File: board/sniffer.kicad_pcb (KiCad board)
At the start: 8 copper layers, 154 x 125 mm, 314 parts, among them J1 BARREL, J10 CONN_SFP_HOST, J11 SFP_CAGE, J12 PMOD_HOST, J13 CONN_SATA_DEVICE, J14 CONN_SATA_HOST, J15 CONN_LVDS_EXPANSION_HOST, J2 32K243-40ML5, J3 BEL_FUSE_0826-1G1T-23-F, J4 XILINX_JTAG, J5 32K243-40ML5, J6 32K243-40ML5, J7 32K243-40ML5, J8 CONN_SFF8087, J9 CONN_SFF8087, M1 SCREW_HOLE, M2 SCREW_HOLE, M3 SCREW_HOLE, M4 SCREW_HOLE, Q1 SSM6N58NU, U1 OKL-T_3-W12P-C, U10 KSZ9031RN, U11 74AVCH1T45, U12 74AVCH1T45, U13 74AVCH1T45, U14 74AVCH1T45, U15 W25Q128JV, U16 FPF2498, U17 FPF2498, U18 LP2996A, U2 LTC3374-QFN, U3 MYTNA1R84RELA2RA, U4 DDR3_SODIMM, U5 XC7K70T-2FBG484, U6 ECX2-LMV-7CN-156.250-TR, U7 ECX2-LMV-3CN-125.000-TR, U8 ECX2-LMV-3CN-125.000-TR, U9 ECS-2016MVQ-250-CN

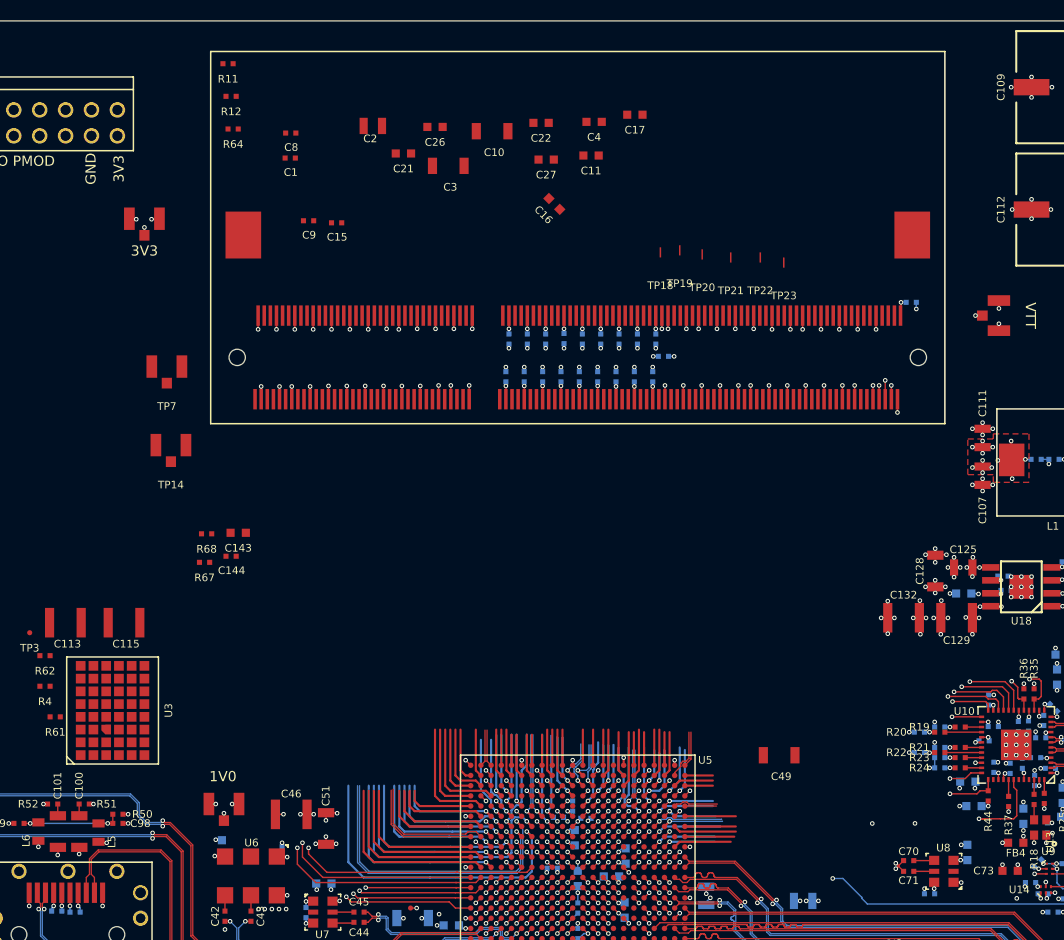
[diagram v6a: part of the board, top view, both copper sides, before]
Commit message: Preliminary layout of DQ byte groups 3:0 on DDR3. Not length matched.
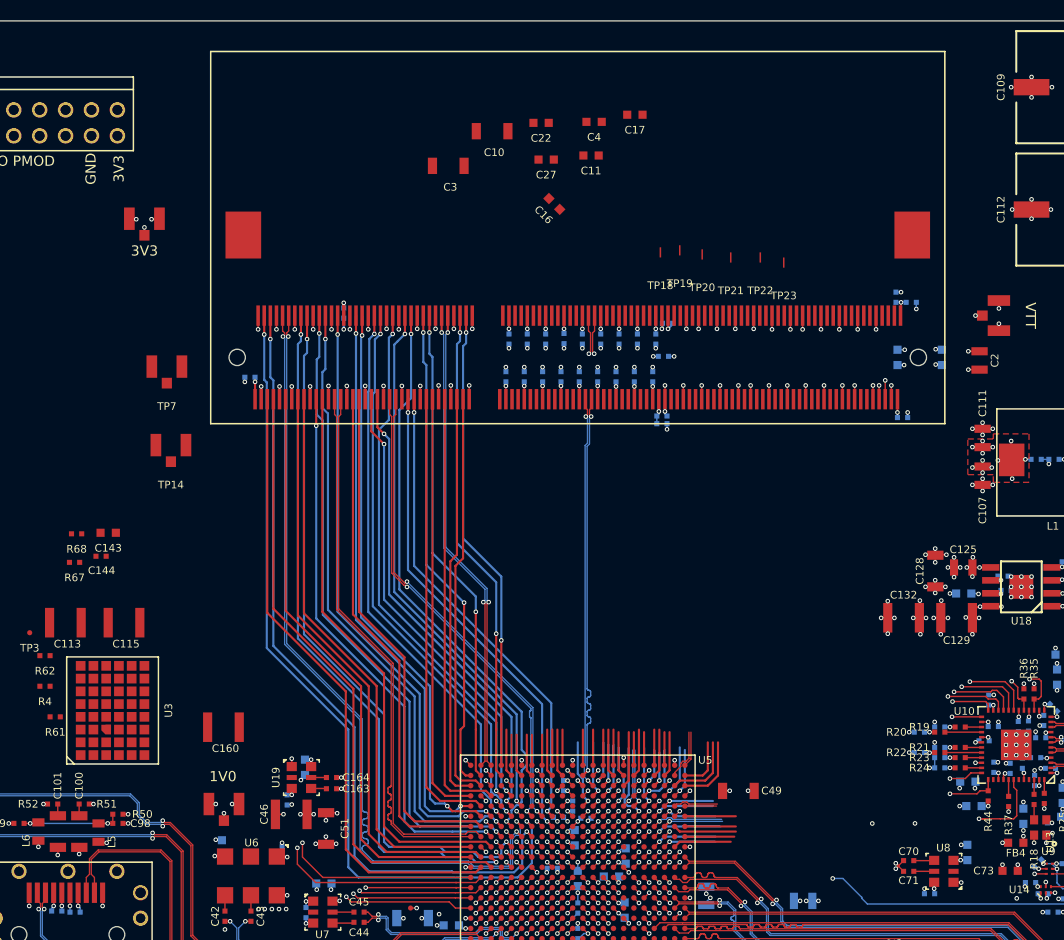
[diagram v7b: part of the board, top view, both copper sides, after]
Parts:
- added C160: DNP, azonenberg_pcb:EIA_1210_CAP_NOSILK, F.Cu at (74.2, 102.2)
- added C161: 4.7 uF, azonenberg_pcb:EIA_0603_CAP_NOSILK, B.Cu at (82.2, 106.2)
- added C162: 0.47 uF, azonenberg_pcb:EIA_0402_CAP_NOSILK, B.Cu at (80.5, 109.4)
- added C163: 0.1 uF, azonenberg_pcb:EIA_0402_CAP_NOSILK, F.Cu at (84.8, 108.3)
- added C164: 0.1 uF, azonenberg_pcb:EIA_0402_CAP_NOSILK, F.Cu at (84.8, 107.2)
- added R75: 100, azonenberg_pcb:EIA_0402_RES_NOSILK, B.Cu at (107.6, 108.0)
- added U19: SIT9121AI-2BF-XXS200.000000G, azonenberg_pcb:OSCILLATOR_LVDS_3.2x2.5, F.Cu at (81.9, 107.2)
- C1, C15, C21, C26, C8, C9, R11, R12, R64: moved to B.Cu
- U7: value ECX2-LMV-3CN-125.000-TR -> SIT9121AI-2BF-XXS200.000000G
- moved C2 63.8 mm to (148.4, 66.3), turned to 90 degrees
- moved C15 58.7 mm to (140.8, 71.9)
- moved C9 58.1 mm to (140.2, 60.1), turned to 90 degrees
- moved R11 55.3 mm to (117.3, 72.5), turned to 180 degrees
- moved C26 54.6 mm to (144.7, 66.0), turned to 90 degrees
- moved R12 52.6 mm to (117.2, 71.8), turned to 180 degrees
- moved C21 52.4 mm to (140.3, 66.0), turned to 90 degrees
- moved C8 41.4 mm to (117.8, 62.6)
- moved C1 21.9 mm to (76.8, 68.0), turned to 180 degrees
- moved R64 21.1 mm to (86.0, 61.6), turned to 270 degrees
- moved R67 12.8 mm to (59.6, 86.1)
- moved C143 12.8 mm to (63.0, 83.2)
- moved C144 12.8 mm to (62.2, 85.5)
- moved R68 12.7 mm to (59.9, 83.3)
- moved C49 5.32 mm to (124.8, 108.5)
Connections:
- net /SERDES interfaces/REFCLK_125_AC_N renamed /SERDES interfaces/REFCLK_200_AC_N
- net /SERDES interfaces/REFCLK_125_AC_P renamed /SERDES interfaces/REFCLK_200_AC_P
- net /SERDES interfaces/REFCLK_125_N renamed /SERDES interfaces/REFCLK_200_N
- net /SERDES interfaces/REFCLK_125_P renamed /SERDES interfaces/REFCLK_200_P
- U5 pad A13: /DDR/RAM_DQ0_3 -> /DDR/RAM_DM0
- U5 pad A14: /DDR/RAM_DQ0_4 -> /DDR/RAM_DQ0_3
- U5 pad A18: /DDR/RAM_DQ1_4 -> /DDR/RAM_DQ1_6
- U5 pad A21: /DDR/RAM_DQ3_3 -> /DDR/RAM_DQ3_4
- U5 pad B12: /DDR/RAM_DQ0_2 -> /DDR/RAM_DQ0_0
- U5 pad B13: /DDR/RAM_DQ0_6 -> /DDR/RAM_DQ0_2
- U5 pad B16: /DDR/RAM_DQ1_1 -> /DDR/RAM_DQ1_3
- U5 pad B17: /DDR/RAM_DQ1_3 -> /DDR/RAM_DQ1_7
- U5 pad B20: /DDR/RAM_DQ3_6 -> /DDR/RAM_DQ3_3
- U5 pad B21: /DDR/RAM_DQ3_7 -> /DDR/RAM_DQ3_5
- U5 pad C13: /DDR/RAM_DQ0_5 -> /DDR/RAM_DQ0_6
- U5 pad C14: /DDR/RAM_DM1 -> /DDR/RAM_DQ1_1
- U5 pad C17: /DDR/RAM_DQ1_7 -> /DDR/RAM_DM1
- U5 pad D15: /DDR/RAM_DQ1_5 -> /DDR/RAM_DQ1_4
- U5 pad D16: /DDR/RAM_DQ1_6 -> /DDR/RAM_DQ1_5
- U5 pad D17: /DDR/RAM_DQ2_2 -> /DDR/RAM_DQ2_4
- U5 pad D19: /DDR/RAM_DQ2_7 -> /DDR/RAM_DM2
- U5 pad D21: /DDR/RAM_DQ3_4 -> /DDR/RAM_DQ3_6
- U5 pad D22: /DDR/RAM_DQ3_5 -> /DDR/RAM_DQ3_7
- U5 pad E16: /DDR/RAM_DQ2_1 -> /DDR/RAM_DQ2_7
- U5 pad E17: /DDR/RAM_DM2 -> /DDR/RAM_DQ2_5
- U5 pad E18: /DDR/RAM_DQ2_0 -> /DDR/RAM_DQ2_1
- U5 pad E19: /DDR/RAM_DQ2_6 -> /DDR/RAM_DQ2_0
- U5 pad F18: /DDR/RAM_DQ2_5 -> /DDR/RAM_DQ2_6
- U5 pad G15: /DDR/RAM_DM0 -> /DDR/RAM_DQ0_5
- U5 pad G16: /DDR/RAM_DQ0_0 -> /DDR/RAM_DQ0_4
- U5 pad J16: /DDR/RAM_DQ2_3 -> /DDR/RAM_DQ2_2
- U5 pad J17: /DDR/RAM_DQ2_4 -> /DDR/RAM_DQ2_3
- U5 pad L19: /DDR/RAM_A10 -> /DDR/CLK_200_AC_P
- U5 pad L20: /DDR/RAM_A11 -> /DDR/CLK_200_AC_N
- U5 pad R21: (no net) -> /DDR/RAM_A10
- U5 pad R22: (no net) -> /DDR/RAM_A11
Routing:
- net /DDR/RAM_DQ0_4: track 13.9 -> 81.5 mm, vias 0 -> 2
- net /DDR/RAM_DQ0_5: track 17.9 -> 78.0 mm, vias 1 -> 2
- net /DDR/RAM_DQ1_4: track 6.71 -> 62.8 mm, vias 0 -> 2
- net /DDR/RAM_DQ0_6: track 16.4 -> 68.3 mm, vias 0 -> 2
- net /DDR/RAM_DQ0_7: track 18.6 -> 69.4 mm, vias 1 -> 2
- net /DDR/RAM_DQ2_7: track 6.21 -> 56.9 mm, vias 1 -> 2
- net /DDR/RAM_DQS0_P: track 28.2 -> 77.2 mm, vias 1 -> 2
- net /DDR/RAM_DQ1_5: track 13.6 -> 62.0 mm, vias 1 -> 2
- net /DDR/RAM_DQ2_5: track 7.21 -> 55.2 mm, vias 1 -> 2
- net /DDR/RAM_DQ2_6: track 6.41 -> 53.7 mm, vias 1 -> 2
- net /DDR/RAM_DQS0_N: track 29.9 -> 77.2 mm, vias 1 -> 2
- net /DDR/RAM_DQ2_4: track 8.27 -> 54.8 mm, vias 1 -> 2
- net /DDR/RAM_DQ1_7: track 9.91 -> 55.9 mm, vias 1 -> 2
- net /DDR/RAM_DQ1_1: track 10.1 -> 55.7 mm
- net /DDR/RAM_DM1: track 14.6 -> 59.4 mm, vias 1 -> 2
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
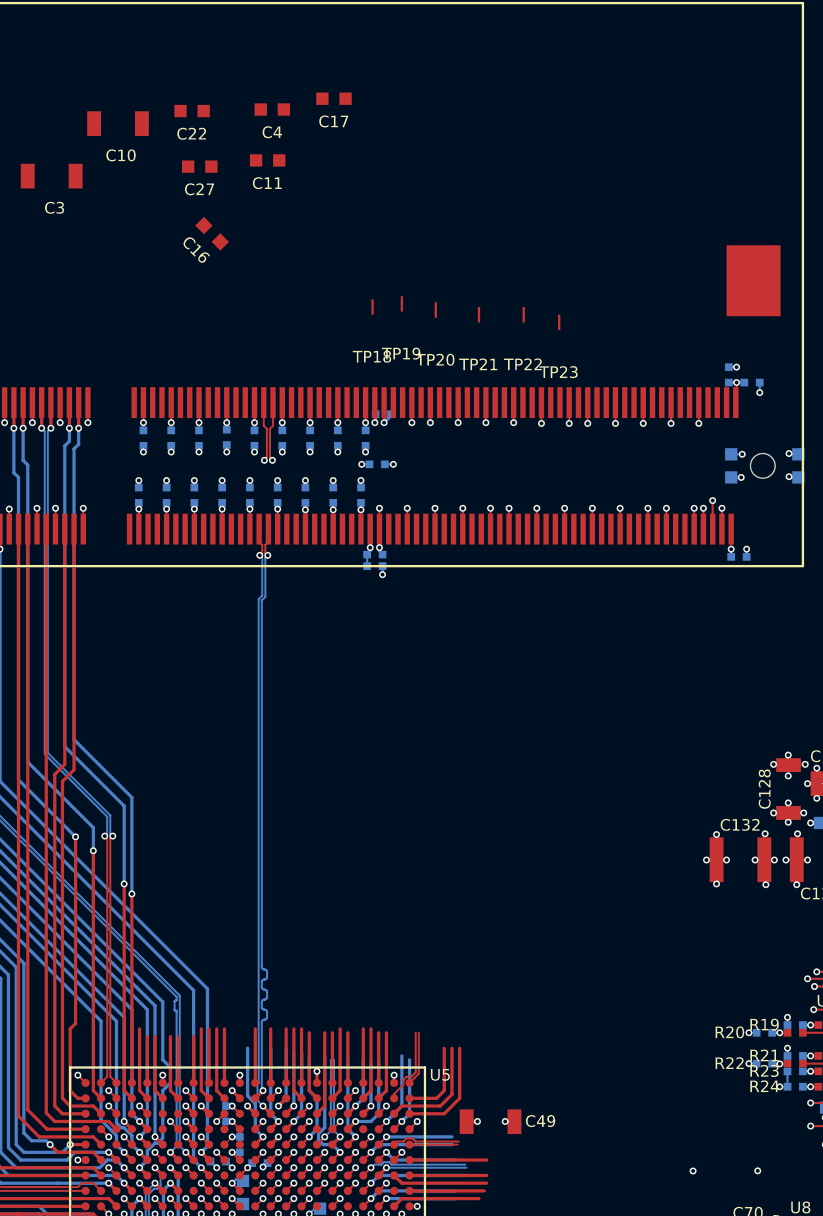
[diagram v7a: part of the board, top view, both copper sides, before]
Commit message: Finished initial routing of DDR C/A bus
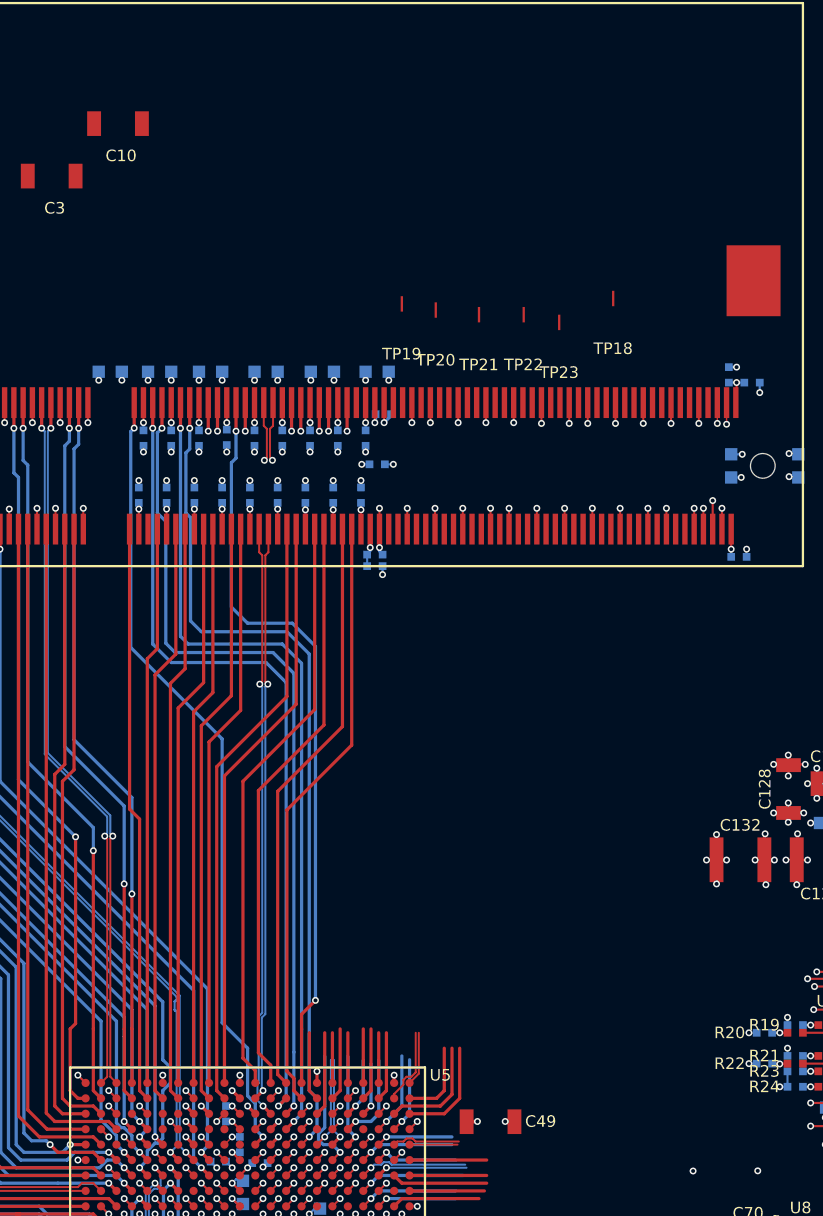
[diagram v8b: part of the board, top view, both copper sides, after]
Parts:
- C11, C16, C17, C22, C27, C4: moved to B.Cu
- moved C17 22.9 mm to (100.1, 59.9)
- moved C22 18.9 mm to (113.8, 59.9)
- moved C4 18.3 mm to (117.4, 59.9)
- moved TP18 15.6 mm to (132.7, 55.1)
- moved C11 13.7 mm to (110.2, 59.9)
- moved C27 13.3 mm to (106.6, 59.9)
- moved C16 9.57 mm to (103.3, 59.9), turned to 180 degrees
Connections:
- U5 pad E21: /DDR/RAM_A0 -> /DDR/RAM_CKE0
- U5 pad E22: /DDR/RAM_A1 -> /DDR/RAM_BA2
- U5 pad F21: /DDR/RAM_A5 -> /DDR/RAM_A12
- U5 pad G21: /DDR/RAM_A4 -> /DDR/RAM_A9
- U5 pad G22: /DDR/RAM_A3 -> /DDR/RAM_A8
- U5 pad H20: /DDR/RAM_A9 -> /DDR/RAM_A6
- U5 pad H22: /DDR/RAM_A2 -> /DDR/RAM_A5
- U5 pad J20: /DDR/RAM_A8 -> /DDR/RAM_A4
- U5 pad J21: /DDR/RAM_A6 -> /DDR/RAM_A3
- U5 pad J22: /DDR/RAM_A7 -> /DDR/RAM_A1
- U5 pad K21: /DDR/RAM_BA0 -> /DDR/RAM_A10
- U5 pad K22: /DDR/RAM_RESET_N -> /DDR/RAM_BA0
- U5 pad M17: /DDR/RAM_A14 -> /DDR/RAM_A0
- U5 pad M18: /DDR/RAM_A15 -> /DDR/RAM_CKE1
- U5 pad M22: /DDR/RAM_BA1 -> /DDR/RAM_WE_N
- U5 pad N17: /DDR/RAM_RAS_N -> /DDR/RAM_BA1
- U5 pad N18: /DDR/RAM_A12 -> /DDR/RAM_RAS_N
- U5 pad N19: /DDR/RAM_A13 -> /DDR/RAM_RESET_N
- U5 pad N22: /DDR/RAM_BA2 -> /DDR/RAM_CAS_N
- U5 pad P16: /DDR/RAM_CAS_N -> /DDR/RAM_CS0_N
- U5 pad P19: /DDR/RAM_CKE1 -> /DDR/RAM_A11
- U5 pad P20: /DDR/RAM_CS0_N -> /DDR/RAM_A14
- U5 pad P21: /DDR/RAM_ODT1 -> /DDR/RAM_A15
- U5 pad P22: /DDR/RAM_WE_N -> /DDR/RAM_A13
- U5 pad R17: /DDR/RAM_CS1_N -> /DDR/RAM_ODT1
- U5 pad R18: /DDR/RAM_CKE0 -> /DDR/RAM_A7
- U5 pad R21: /DDR/RAM_A10 -> /DDR/RAM_CS1_N
- U5 pad R22: /DDR/RAM_A11 -> /DDR/RAM_A2
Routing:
- net /RAM_SDA: track 27.9 -> 97.9 mm, vias 1 -> 2
- net /RAM_SCL: track 27.5 -> 97.2 mm, vias 1 -> 2
- net /DDR/RAM_RESET_N: track 5.25 -> 61.8 mm, vias 1 -> 2
- net /DDR/RAM_A7: track 3.50 -> 55.4 mm, vias 0 -> 2
- net /DDR/RAM_A11: track 3.50 -> 54.3 mm, vias 0 -> 2
- net /DDR/RAM_BA1: track 3.50 -> 51.9 mm, vias 0 -> 2
- net /DDR/RAM_A0: track 4.71 -> 52.7 mm, vias 0 -> 2
- net /DDR/RAM_CS0_N: track 4.21 -> 51.4 mm, vias 1 -> 2
- net /DDR/RAM_A15: track 6.87 -> 53.7 mm, vias 1 -> 2
- net /DDR/RAM_CKE1: track 5.41 -> 52.0 mm, vias 1 -> 2
- net /DDR/RAM_ODT1: track 4.66 -> 50.7 mm, vias 1 -> 2
- net /DDR/RAM_A2: track 3.00 -> 48.6 mm, vias 0 -> 2
- net /DDR/RAM_A14: track 8.75 -> 53.8 mm, vias 1 -> 2
- net /DDR/RAM_A4: track 4.21 -> 46.7 mm, vias 0 -> 2
- net /DDR/RAM_ODT0: track 7.91 -> 50.4 mm, vias 1 -> 2
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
